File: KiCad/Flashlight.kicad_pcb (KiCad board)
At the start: 2 copper layers, 58.7 x 106.4 mm, 75 parts, among them J3 XT30PW-F, J4 ICSP 1x6, K1 HFD4-24-SR, Q1 PMOS_Vin, Q2 CSD25402Q3A, Q3 Q_NMOS_GSD, Q4 Q_NMOS_GSD, SW1 SW_SPST, SW2 SW_Push, U1 AMS1117-5.0, U2 PIC16F716-ISO, U3 LM60BIM3, U4 LM25085SD_NOPB, Y1 Crystal

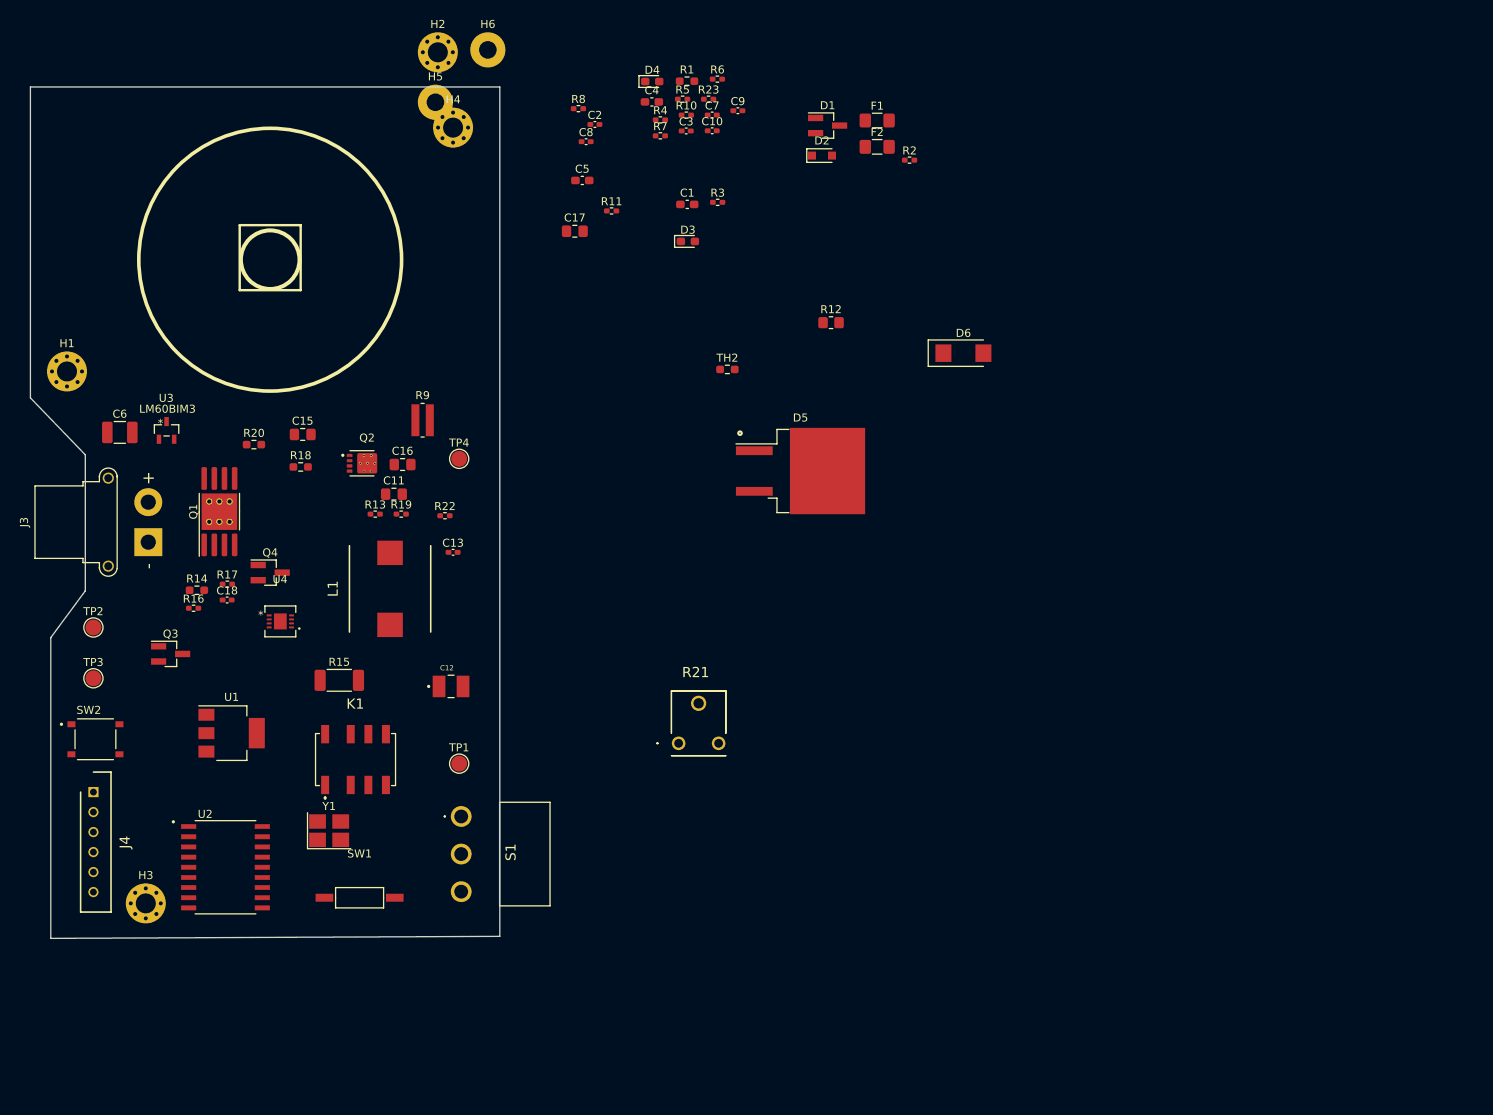
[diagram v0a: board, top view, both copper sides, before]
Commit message: Finished routing the first version of a PCB. WSON is out of stock so new driver was used.
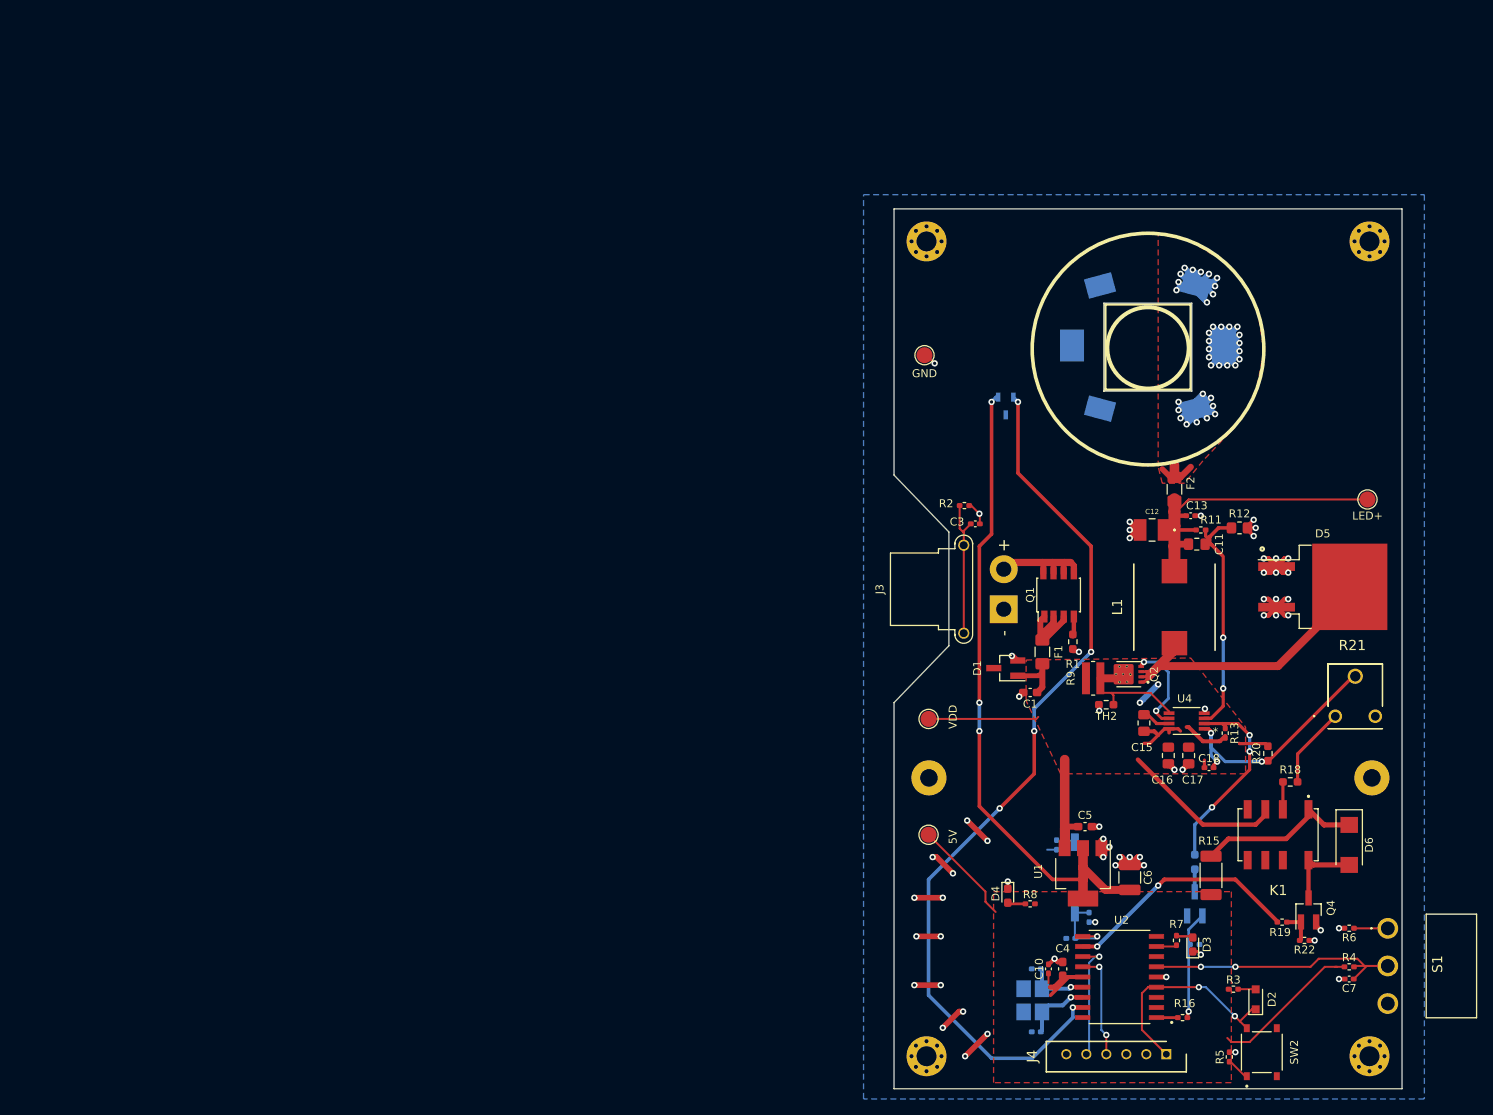
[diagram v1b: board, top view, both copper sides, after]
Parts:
- added J2: XHP90, Flashlight:XHP90, B.Cu at (223.0, 53.3)
- C2, C8, C9, Q3, R10, R14, R17, R23, SW1, U3, Y1: moved to B.Cu
- Q1: footprint Package_SO:SOP-8-1EP_4.57x4.57mm_P1.27mm_EP4.57x4.45mm_ThermalVias -> Flashlight:YJS4407A
- R2: value R -> 10k
- U4: value LM25085SD_NOPB -> LM25085MM_NOPB; footprint Flashlight:LM25085SD&slash_NOPB -> Flashlight:LM25085MM&slash_NOPB
- moved H1 183.9 mm to (250.7, 142.0)
- moved SW2 151.0 mm to (237.2, 141.5), turned to 90 degrees
- moved H6 143.2 mm to (251.0, 107.2)
- moved J4 138.1 mm to (225.3, 141.7), turned to 180 degrees
- moved C6 138.0 mm to (220.7, 119.6), turned to 90 degrees
- moved R5 137.9 mm to (233.2, 142.1), turned to 90 degrees
- moved Q4 136.5 mm to (243.1, 123.7), turned to 90 degrees
- moved R4 136.5 mm to (248.2, 130.8)
- moved C7 134.2 mm to (248.2, 132.3), turned to 180 degrees
- moved R16 133.8 mm to (227.3, 137.2), turned to 180 degrees
- moved R20 132.5 mm to (238.0, 104.1), turned to 90 degrees
- moved R6 132.3 mm to (248.2, 126.0), turned to 180 degrees
- moved Q3 131.8 mm to (228.9, 122.9), turned to 90 degrees
- moved R18 129.8 mm to (240.8, 107.7), turned to 180 degrees
- moved R14 129.3 mm to (228.9, 117.7), turned to 90 degrees
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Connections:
- C15 pad 1: VIN -> Net-(C15-Pad1)
- C15 pad 2: Net-(C15-Pad2) -> VIN
- C3 pad 1: LED_GND -> Net-(C3-Pad1)
- C3 pad 2: Net-(C3-Pad2) -> LED_GND
- Q1 pad 1: VXT -> Net-(F1-Pad2)
- Q1 pad 2: Net-(Q1-Pad2) -> Net-(F1-Pad2)
- Q1 pad 4: (no net) -> Net-(Q1-Pad4)
- Q1 pad 5: (no net) -> VXT
- Q1 pad 6: (no net) -> VXT
- Q1 pad 7: (no net) -> VXT
- Q1 pad 8: (no net) -> VXT
- Q2 pad 9_1: (no net) -> ISEN
- Q2 pad 9_2: (no net) -> ISEN
- Q2 pad 9_3: (no net) -> ISEN
- Q2 pad 9_4: (no net) -> ISEN
- Q2 pad 9_5: (no net) -> ISEN
- Q2 pad 9_6: (no net) -> ISEN
- Q2 pad 9_7: (no net) -> ISEN
- R1 pad 2: Net-(Q1-Pad2) -> Net-(Q1-Pad4)
- R2 pad 1: LED_GND -> Net-(C3-Pad1)
- R2 pad 2: Net-(C3-Pad2) -> LED_GND
- U4 pad 7: Net-(C15-Pad2) -> Net-(C15-Pad1)
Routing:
- net +5V: track 0.00 -> 126.3 mm, vias 0 -> 4
- net ANALOG_TEMP: track 0.00 -> 113.4 mm, vias 0 -> 5
- net Net-(F2-Pad1): track 0.00 -> 97.6 mm, vias 0 -> 37
- net LED_GND: track 0.00 -> 86.6 mm, vias 0 -> 60
- net VIN: track 0.00 -> 80.0 mm, vias 0 -> 2
- net Net-(D5-Pad4): track 0.00 -> 50.3 mm
- net LED_VDD: track 0.00 -> 41.6 mm
- net MODE: track 0.00 -> 33.9 mm, vias 0 -> 2
- net ADJ: track 0.00 -> 31.3 mm, vias 0 -> 3
- net FB: track 0.00 -> 30.3 mm, vias 0 -> 2
- net RELAY: track 0.00 -> 30.1 mm, vias 0 -> 2
- net VPP\RST: track 0.00 -> 27.0 mm, vias 0 -> 2
- net RT: track 0.00 -> 24.9 mm, vias 0 -> 3
- net Net-(D6-Pad1): track 0.00 -> 21.0 mm
- net Net-(C3-Pad1): track 0.00 -> 17.6 mm
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- added copper zone on F.Cu, net +5V
- added copper zone on B.Cu, net LED_GND
- added copper zone on F.Cu, net Net-(F2-Pad1)
- added copper zone on F.Cu, net VIN
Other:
- board size 58.7 x 106.4 mm -> 63.5 x 110 mm
